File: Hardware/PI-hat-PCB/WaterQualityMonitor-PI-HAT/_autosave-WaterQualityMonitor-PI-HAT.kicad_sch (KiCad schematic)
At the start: 7 parts

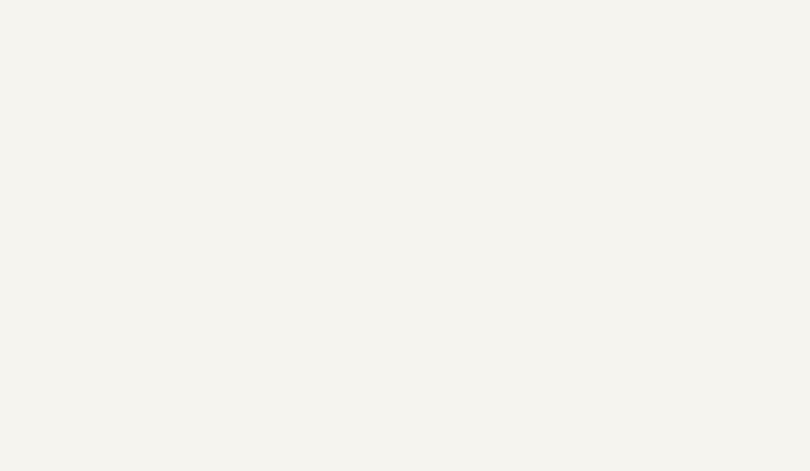
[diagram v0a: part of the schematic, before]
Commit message: removed old regulator circuits
a better chip (tested) has been found rt7272a
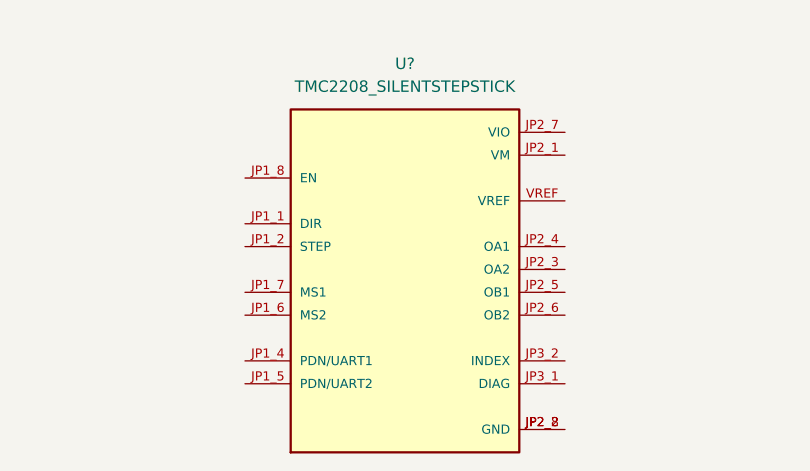
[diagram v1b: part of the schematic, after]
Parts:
- added U?: TMC2208_SILENTSTEPSTICK, MODULE_TMC2208_SILENTSTEPSTICK, symbol TMC2208_SILENTSTEPSTICK:TMC2208_SILENTSTEPSTICK
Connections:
- new net: U?.JP2_2 (GND), U?.JP2_8 (GND)
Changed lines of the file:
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@@
     (pin "2")
+  )
+  (symbol (lib_id "TMC2208_SILENTSTEPSTICK:TMC2208_SILENTSTEPSTICK") (at 138.43 40.64 0) (unit 1)
+    (in_bom yes) (on_board yes) (fields_autoplaced)
+    (property "Reference" "U?" (id 0) (at 138.43 17.78 0))
+    (property "Value" "TMC2208_SILENTSTEPSTICK" (id 1) (at 138.43 20.32 0))
+    (property "Footprint" "MODULE_TMC2208_SILENTSTEPSTICK" (id 2) (at 138.43 40.64 0)
+      (effects (font (size 1.27 1.27)) (justify left bottom) hide)
+    )
+    (property "Datasheet" "" (id 3) (at 138.43 40.64 0)
+      (effects (font (size 1.27 1.27)) (justify left bottom) hide)
+    )
+    (property "MANUFACTURER" "Trinamic Motion" (id 4) (at 138.43 40.64 0)
+      (effects (font (size 1.27 1.27)) (justify left bottom) hide)
+    )
+    (pin "JP1_1")
+    (pin "JP1_2")
+    (pin "JP1_4")
+    (pin "JP1_5")
+    (pin "JP1_6")
+    (pin "JP1_7")
+    (pin "JP1_8")
+    (pin "JP2_1")
+    (pin "JP2_2")
+    (pin "JP2_3")
+    (pin "JP2_4")
+    (pin "JP2_5")
+    (pin "JP2_6")
+    (pin "JP2_7")
+    (pin "JP2_8")
+    (pin "JP3_1")
+    (pin "JP3_2")
+    (pin "VREF")
   )
   (symbol (lib_id "pspice:INDUCTOR") (at 46.99 24.13 0) (unit 1)
@@
       (reference "R?") (unit 1) (value "5.1") (footprint "")
     )
+    (path "/b680e596-746f-4319-b715-ea56e1025124"
+      (reference "U?") (unit 1) (value "TMC2208_SILENTSTEPSTICK") (footprint "MODULE_TMC2208_SILENTSTEPSTICK")
+    )
     (path "/bbc78703-4635-423a-a285-0138bfaaab5c"
